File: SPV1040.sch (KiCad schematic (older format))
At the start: 14 parts

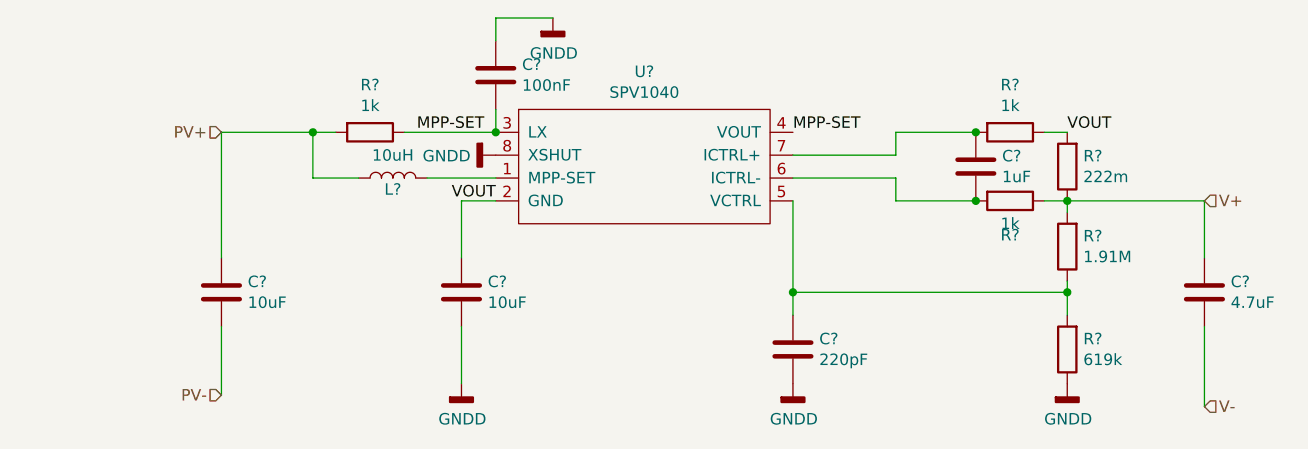
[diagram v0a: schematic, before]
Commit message: Updated SPV1040 added two diodes
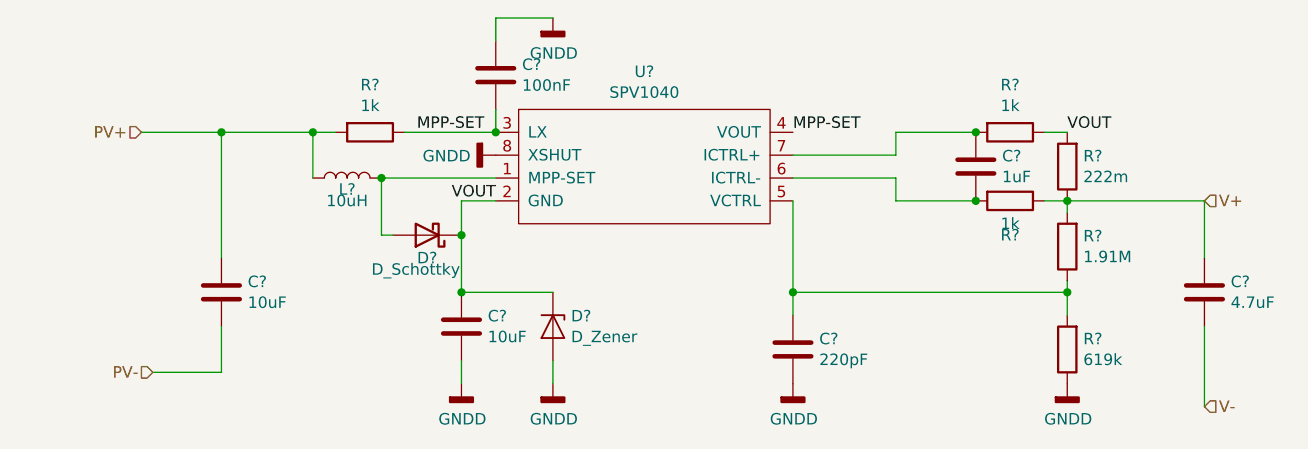
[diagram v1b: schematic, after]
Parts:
- added D?: D_Schottky, symbol Device:D_Schottky
- added D?: D_Zener, symbol Device:D_Zener
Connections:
- net GNDD: now also D?.2 (A)
- net VOUT: now also D?.1 (K), D?.1 (K)
- net at L?.2, U?.1 (MPP-SET): now also D?.2 (A)
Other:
- moved on the sheet: C?, L?
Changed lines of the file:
@@
 $Descr A4 11693 8268
 encoding utf-8
-Sheet 20 34
+Sheet 3 34
 Title "Electrical Power System"
 Date "2019-04-25"
@@
 	4550 3500 4650 3500
 Wire Wire Line
-	4550 3700 4750 3700
-Wire Wire Line
-	5050 3700 5350 3700
-Wire Wire Line
 	7100 3600 7100 3500
 Wire Wire Line
@@
 	7850 3800 8450 3800
 Wire Wire Line
-	5200 4600 5200 4350
-Wire Wire Line
-	5200 4050 5200 3800
-Wire Wire Line
 	4150 3500 4150 4050
-Text HLabel 4150 3500 0    50   Input ~ 0
+Text HLabel 3800 3500 0    50   Input ~ 0
 PV+
-Text HLabel 4150 4650 0    50   Input ~ 0
+Text HLabel 3850 4550 0    50   Input ~ 0
 PV-
 Wire Wire Line
@@
 L Device:L L?
 U 1 1 5CCCC1D3
-P 4900 3700
+P 4700 3700
 AR Path="/5CC6D79E/5CC8FD75/5CCCC1D3" Ref="L?"  Part="1"
 AR Path="/5CC6D79E/5CCAFF7B/5CCCC1D3" Ref="L?"  Part="1"
@@
 AR Path="/5CC6D79E/5CC9E1D4/5CCCC1D3" Ref="L?"  Part="1"
 AR Path="/5CC6D79E/5CCB4B5E/5CCCC1D3" Ref="L?"  Part="1"
-F 0 "L?" V 4850 3700 50  0000 C CNN
-F 1 "10uH" V 4999 3700 50  0000 C CNN
-F 2 "" H 4900 3700 50  0001 C CNN
-F 3 "~" H 4900 3700 50  0001 C CNN
-	1    4900 3700
+F 0 "L?" V 4650 3700 50  0000 C CNN
+F 1 "10uH" V 4600 3700 50  0000 C CNN
+F 2 "" H 4700 3700 50  0001 C CNN
+F 3 "~" H 4700 3700 50  0001 C CNN
+	1    4700 3700
 	0    -1   -1   0
 $EndComp
@@
 L Device:C C?
 U 1 1 5CCCE41F
-P 5200 4200
+P 5200 4350
 AR Path="/5CC6D79E/5CC8FD75/5CCCE41F" Ref="C?"  Part="1"
 AR Path="/5CC6D79E/5CCAFF7B/5CCCE41F" Ref="C?"  Part="1"
@@
 AR Path="/5CC6D79E/5CC9E1D4/5CCCE41F" Ref="C?"  Part="1"
 AR Path="/5CC6D79E/5CCB4B5E/5CCCE41F" Ref="C?"  Part="1"
-F 0 "C?" H 5315 4246 50  0000 L CNN
-F 1 "10uF" H 5315 4155 50  0000 L CNN
-F 2 "" H 5238 4050 50  0001 C CNN
-F 3 "~" H 5200 4200 50  0001 C CNN
-	1    5200 4200
+F 0 "C?" H 5315 4396 50  0000 L CNN
+F 1 "10uF" H 5315 4305 50  0000 L CNN
+F 2 "" H 5238 4200 50  0001 C CNN
+F 3 "~" H 5200 4350 50  0001 C CNN
+	1    5200 4350
 	1    0    0    -1
 $EndComp
@@
 	5350 3000 5350 3100
 Wire Wire Line
-	4150 4350 4150 4650
-Wire Wire Line
 	8450 4350 8450 4700
+$Comp
+L Device:D_Schottky D?
+U 1 1 5D11DAAA
+P 5050 3950
+F 0 "D?" H 5050 4050 50  0000 C CNN
+F 1 "D_Schottky" H 5100 4100 50  0000 C CNN
+F 2 "" H 5050 3950 50  0001 C CNN
+F 3 "~" H 5050 3950 50  0001 C CNN
+	1    5050 3950
+	-1   0    0    1
+$EndComp
+Connection ~ 5200 3950
+Wire Wire Line
+	5200 3950 5200 3800
+Wire Wire Line
+	4900 3950 4850 3950
+Wire Wire Line
+	4850 3950 4850 3700
+Wire Wire Line
+	4850 3700 5350 3700
+Connection ~ 4850 3700
+$Comp
+L Device:D_Zener D?
+U 1 1 5D120B71
+P 5600 4350
+F 0 "D?" V 5554 4429 50  0000 L CNN
+F 1 "D_Zener" V 5645 4429 50  0000 L CNN
+F 2 "" H 5600 4350 50  0001 C CNN
+F 3 "~" H 5600 4350 50  0001 C CNN
+	1    5600 4350
+	0    1    1    0
+$EndComp
+Wire Wire Line
+	5600 4200 5200 4200
+Wire Wire Line
+	5200 3950 5200 4200
+Connection ~ 5200 4200
+Wire Wire Line
+	5200 4500 5200 4600
+$Comp
+L power:GNDD #PWR?
+U 1 1 5D123986
+P 5600 4600
+AR Path="/5CC6D79E/5CC8FD75/5D123986" Ref="#PWR?"  Part="1"
+AR Path="/5CC6D79E/5CCAFF7B/5D123986" Ref="#PWR?"  Part="1"
+AR Path="/5CC6D79E/5CCB70B2/5D123986" Ref="#PWR?"  Part="1"
+AR Path="/5CC6D79E/5CCB7099/5D123986" Ref="#PWR?"  Part="1"
+AR Path="/5CC6D79E/5CC9E1D4/5D123986" Ref="#PWR?"  Part="1"
+AR Path="/5CC6D79E/5CCB4B5E/5D123986" Ref="#PWR?"  Part="1"
+F 0 "#PWR?" H 5600 4350 50  0001 C CNN
+F 1 "GNDD" H 5604 4445 50  0000 C CNN
+F 2 "" H 5600 4600 50  0001 C CNN
+F 3 "" H 5600 4600 50  0001 C CNN
+	1    5600 4600
+	1    0    0    -1
+$EndComp
+Wire Wire Line
+	5600 4500 5600 4600
+Wire Wire Line
+	3800 3500 4150 3500
+Connection ~ 4150 3500
+Wire Wire Line
+	3850 4550 4150 4550
+Wire Wire Line
+	4150 4550 4150 4350
 $EndSCHEMATC

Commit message: Revisions to battery charge and discharge control. SPV1040 now regulates to 4.2V.
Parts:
- removed C?: 100nF, symbol Device:C
- removed C?: 10uF, symbol Device:C
- removed C?: 220pF, symbol Device:C
- removed C?: 1uF, symbol Device:C
- removed D?: D_Schottky, symbol Device:D_Schottky
- removed D?: D_Zener, symbol Device:D_Zener
- removed R? (x2): 1k, symbol Device:R
- removed R?: 222m, symbol Device:R
- removed R?: 1.91M, symbol Device:R
- removed R?: 619k, symbol Device:R
- added C? (x2): 1n, symbol Device:C
- added R?: 768k, symbol Device:R
- added R?: 330k, symbol Device:R
- added SC?: Solar_Cell, symbol Device:Solar_Cell
- C?: value 10uF -> 100u; symbol Device:C -> Main-rescue:C-Device
- C?: value 4.7uF -> 100u; symbol Device:C -> Main-rescue:C-Device
- L?: symbol Device:L -> Main-rescue:L-Device
- R?: symbol Device:R -> Main-rescue:R-Device
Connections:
- net GNDD is gone; now on an unnamed net: U?.8 (XSHUT)
- net PV- is gone; now on net V-: C?.2
- net VOUT is gone; now on net V-: U?.2 (GND)
- net V+: now also U?.4 (VOUT), U?.6 (ICTRL-), U?.7 (ICTRL+), R?.1
- net V-: now also C?.2, C?.2, R?.2, SC?.2 (-)
- net at U?.1 (MPP-SET): now also R?.1, C?.1; no longer L?.2
- net at U?.5 (VCTRL): now also C?.1, R?.1, R?.2
- removed net MPP-SET: R?.1, U?.3 (LX), U?.4 (VOUT)
- net PV+: no longer names the net of C?.1, L?.1, R?.2
- net PV+: now also SC?.1 (+)
- new net: L?.2, U?.3 (LX)
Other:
- note added: "Inductor:\nB82442T1103K050"
- moved on the sheet: C?, L?, R?, U?
